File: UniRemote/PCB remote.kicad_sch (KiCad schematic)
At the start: 20 parts, among them J1 Conn_01x01, J2 Conn_01x01, J3 02_Socket, J4 Conn_01x02_Socket, Q1 PMV28XPEAR, Q2 BSS138, SW1 GREEN, SW2 RED, U1 RFM69HW, U2 SSD1306, U3 Joystick, U4 HW373

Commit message: Har lavet begge pcber om. Remote har ændret struktur for mere håndholdt design og ekstra knapper plus LEDer. roboside har fået ny relay og LEDer
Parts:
- added C5: 100nF, Capacitor_SMD:C_0805_2012Metric_Pad1.18x1.45mm_HandSolder, symbol Device:C
- added D1: LED, LED_SMD:LED_0805_2012Metric_Pad1.15x1.40mm_HandSolder, symbol Device:LED
- added R3: 280, Resistor_SMD:R_0805_2012Metric_Pad1.20x1.40mm_HandSolder, symbol Device:R
- added S2, S3: TL3301TF160QG, Remote-footprints:TL3301TF160QG, symbol Remote-PCB-dele:TL3301TF160QG
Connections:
- net +3.3V: now also R3.1
- net GND: now also S1.4 (MH1), S1.5 (MH2), C5.2, D1.1 (K), S2.3 (NO_1), S2.4 (NO_2), S3.3 (NO_1), S3.4 (NO_2)
- net at C4.1, Q1.1 (G), Q2.3 (D)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: now also S2.1 (COM_1), S2.2 (COM_2)
- net Button: now reaches A1.22 (D10)
- net Button: now also C5.1, S3.1 (COM_1), S3.2 (COM_2)
- net DIO2: now reaches A1.23 (D11)
- net DIO2: now also U1.1 (DIO2)
- net DIO3: now reaches A1.24 (D12)
- net DIO3: now also U1.6 (DIO3)
- new net: D1.2 (A), R3.2
- no-connect marks 18 -> 11
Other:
- moved on the sheet: C4

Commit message: pcb
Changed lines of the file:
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@@
 		(on_board yes)
 		(dnp no)
-		(fields_autoplaced yes)
 		(property "Reference" "S2"
-			(at 262.89 139.6999 90)
+			(at 256.286 158.496 90)
 			(effects
 				(font
@@
 		)
 		(property "Value" "TL3301TF160QG"
-			(at 262.89 142.2399 90)
+			(at 249.936 161.29 90)
 			(effects
 				(font

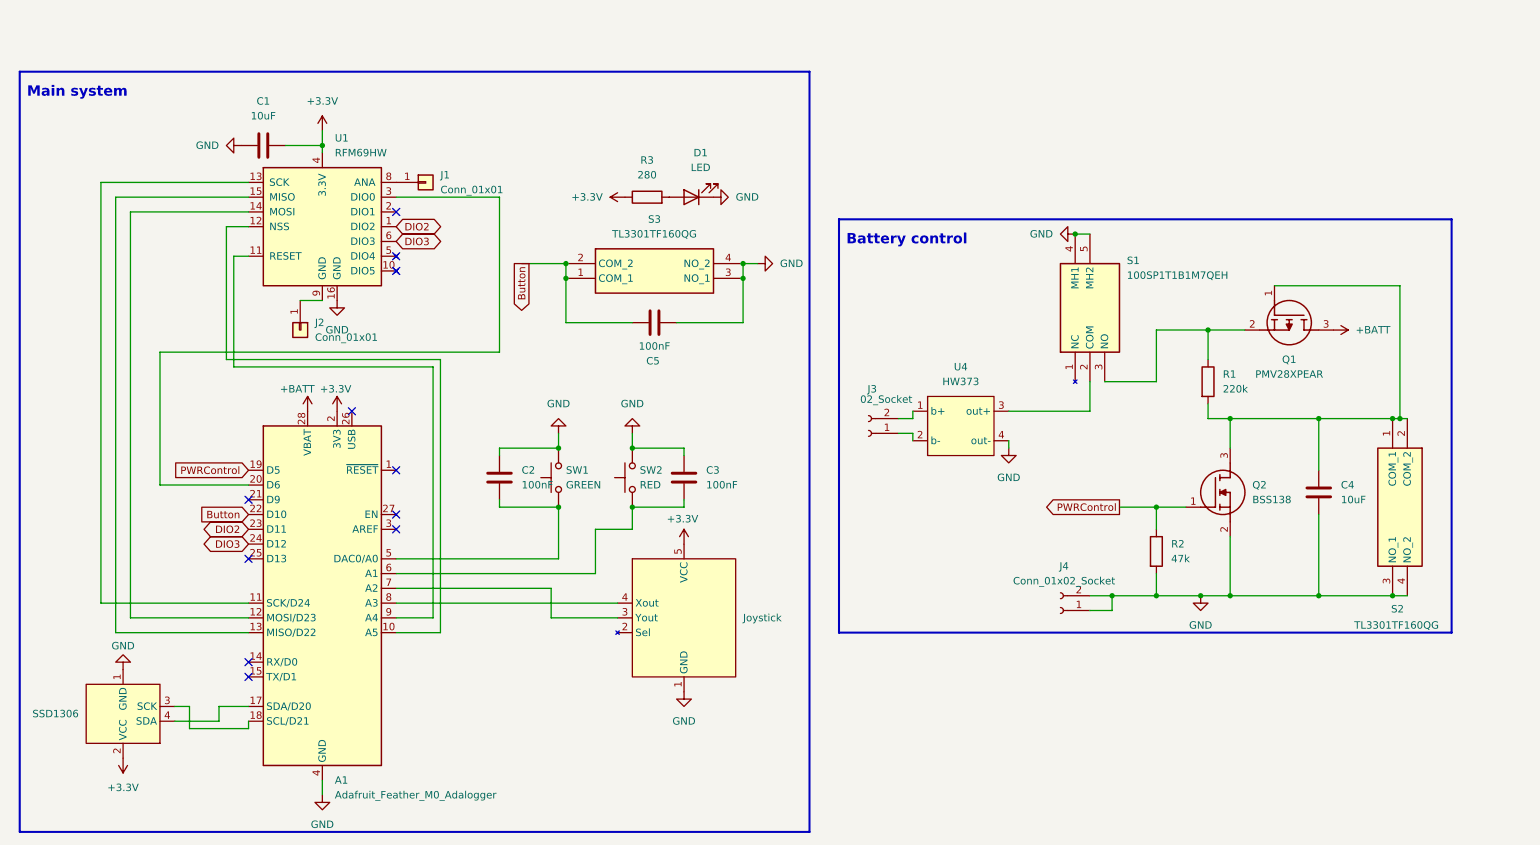
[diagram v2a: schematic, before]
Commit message: Add test scripts, PCB design files, and appendix code listings
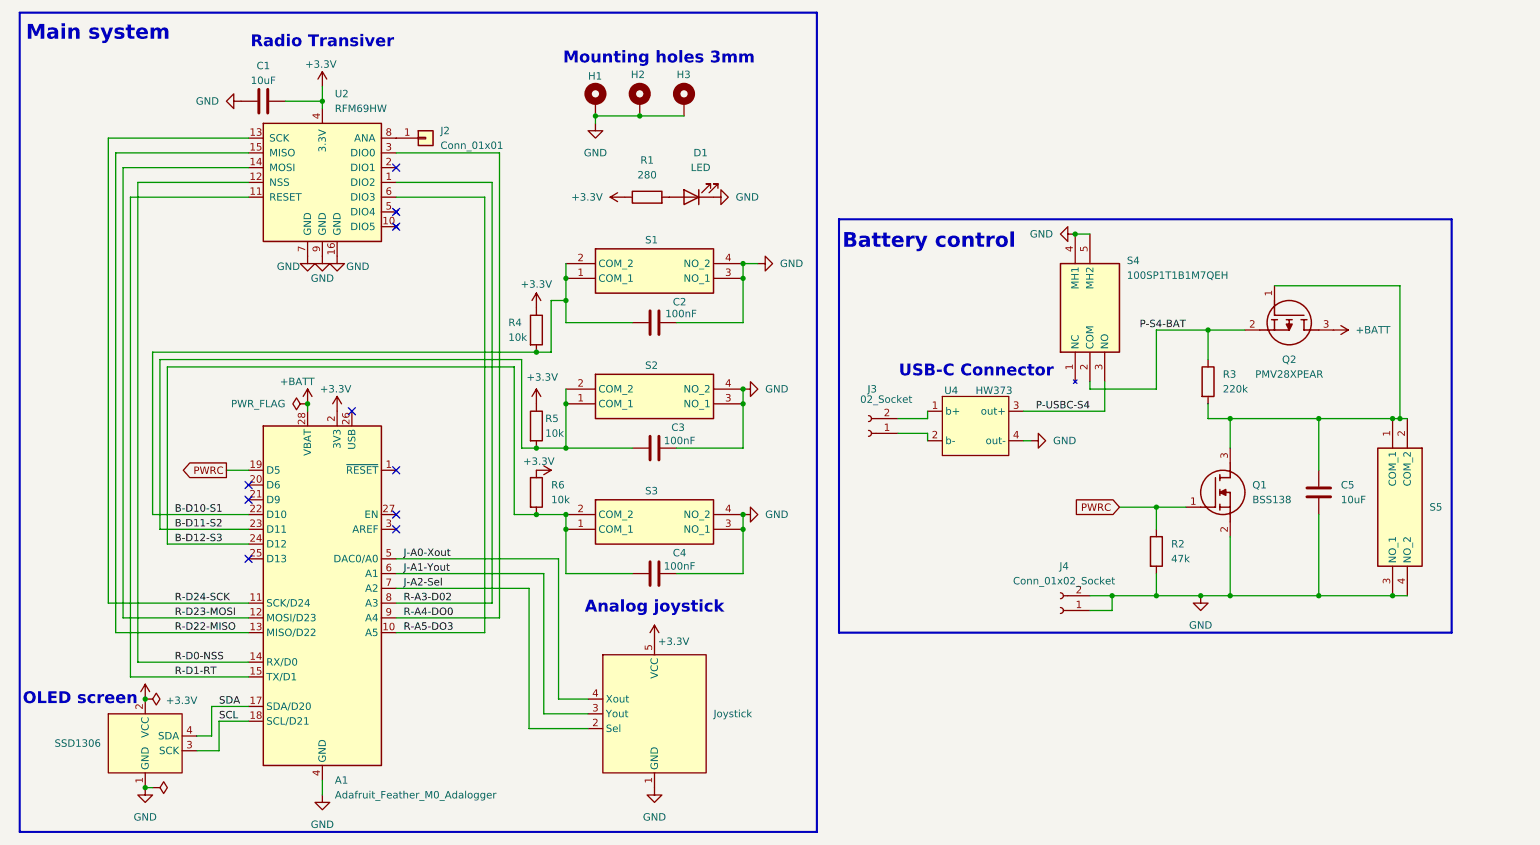
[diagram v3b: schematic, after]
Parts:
- removed J2: Conn_01x01, Connector_PinSocket_2.54mm:PinSocket_1x01_P2.54mm_Vertical, symbol Connector_Generic:Conn_01x01
- removed SW1: GREEN, Connector_PinSocket_2.54mm:PinSocket_1x02_P2.54mm_Vertical, symbol Switch:SW_Push
- removed SW2: RED, Connector_PinSocket_2.54mm:PinSocket_1x02_P2.54mm_Vertical, symbol Switch:SW_Push
- added H1, H2, H3: MountingHole_Pad, MountingHole:MountingHole_3mm_Pad_Via, symbol Mechanical:MountingHole_Pad
- added R4, R5, R6: 10k, Resistor_SMD:R_0805_2012Metric_Pad1.20x1.40mm_HandSolder, symbol Device:R
- added S2, S3: TL3301TF160QG, Remote-footprints:TL3301TF160QG, symbol Remote-PCB-dele:TL3301TF160QG
- renumbered C5 to C2, C2 to C3, C3 to C4, C4 to C5, J1 to J2, Q2 to Q1, Q1 to Q2, R3 to R1, R1 to R3, S3 to S1, S1 to S4, S2 to S5, U2 to U1, U1 to U2
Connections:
- net +3.3V: now also R4.1, R5.1, R6.1
- net GND: now also C3.2, C4.2, U2.7 (GND), U2.9 (GND), H1.1, H2.1, H3.1, S2.3 (NO_1), S2.4 (NO_2), S3.3 (NO_1), S3.4 (NO_2); no longer C3.1, C4.1
- net SCL: now reaches A1.18 (SCL/D21), U1.3 (SCK)
- net SDA: now reaches A1.17 (SDA/D20), U1.4 (SDA)
- net J-A0-Xout: now reaches A1.5 (DAC0/A0)
- net J-A0-Xout: now also U3.4 (Xout); no longer C3.2
- net R-A5-DO3: now reaches A1.10 (A5)
- net R-A5-DO3: now also U2.6 (DIO3); no longer U2.12 (NSS)
- net R-D24-SCK: now reaches A1.11 (SCK/D24), U2.13 (SCK)
- net R-D23-MOSI: now reaches A1.12 (MOSI/D23), U2.14 (MOSI)
- net R-D22-MISO: now reaches A1.13 (MISO/D22), U2.15 (MISO)
- net R-D0-NSS: now reaches A1.14 (RX/D0)
- net R-D0-NSS: now also U2.12 (NSS)
- net R-D1-RT: now reaches A1.15 (TX/D1)
- net R-D1-RT: now also U2.11 (RESET)
- net at A1.20 (D6): no longer U2.3 (DIO0)
- net J-A1-Yout: now reaches A1.6 (A1)
- net J-A1-Yout: now also U3.3 (Yout); no longer C4.2
- net J-A2-Sel: now reaches A1.7 (A2)
- net J-A2-Sel: now also U3.2 (Sel); no longer U3.3 (Yout)
- net R-A3-D02: now reaches A1.8 (A3)
- net R-A3-D02: now also U2.1 (DIO2); no longer U3.4 (Xout)
- net R-A4-DO0: now reaches A1.9 (A4)
- net R-A4-DO0: now also U2.3 (DIO0); no longer U2.11 (RESET)
- net P-S4-BAT: now reaches S4.2 (COM)
- net P-S4-BAT: now also Q2.2 (S), R3.1; no longer U4.3 (out+)
- net Button renamed B-D10-S1
- net B-D10-S1: now also R4.2
- net DIO2 renamed B-D11-S2
- net B-D11-S2: now also C3.1, R5.2, S2.1 (COM_1), S2.2 (COM_2); no longer U2.1 (DIO2)
- net DIO3 renamed B-D12-S3
- net B-D12-S3: now also C4.1, R6.2, S3.1 (COM_1), S3.2 (COM_2); no longer U2.6 (DIO3)
- net PWRControl renamed PWRC
- new net P-USBC-S4: S4.3 (NO), U4.3 (out+)
- no-connect marks 11 -> 10
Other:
- note added: "Analog joystick"
- note added: "Mounting holes 3mm"
- note added: "OLED screen"
- note added: "Radio Transiver"
- note added: "USB-C Connector"
- company: (none) -> DTU Bachelor Elektro
- title: (none) -> UniRomote
- moved on the sheet: C1, C3, C4, J2, U4
